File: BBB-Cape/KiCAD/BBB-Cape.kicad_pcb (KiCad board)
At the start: 2 copper layers, 75.3 x 54.6 mm, 60 parts, among them J1 01x06_Stackable Header, J2 RJ45-TRANSFO, P8 02x23_Stackable Header, P9 02x23_Stackable Header, SW1 W5500_RST, SW2 SYS_RST, SW3 Power, U1 WIZnet W5500, Y1 25MHz

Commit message: BBB for review
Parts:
- removed I2C1_0, I2C2_0: Conn_01x02, Pin_Headers:Pin_Header_Straight_1x02_Pitch2.54mm_SMD_Pin1Left
- removed P8, P9: 02x23_Stackable Header, Pin_Headers:Pin_Header_Straight_2x23_Pitch2.54mm
- added C18: 0.1uF, Capacitors_SMD:C_0805, F.Cu at (198.9, 99.6)
- added C19: 0.1uF, Capacitors_SMD:C_0805, F.Cu at (206.5, 99.6)
- added C20: 10nF, Capacitors_SMD:C_0805, F.Cu at (191.5, 102.0)
- added C21: 22nF, Capacitors_SMD:C_0805, F.Cu at (205.9, 105.2)
- added C22: 4.7uF, Capacitors_SMD:C_0805, F.Cu at (201.4, 99.6)
- added C23: 10nF, Capacitors_SMD:C_0805, F.Cu at (204.0, 99.6)
- added C24: 18pF, Capacitors_SMD:C_0805, F.Cu at (214.5, 95.4)
- added C25: 18pF, Capacitors_SMD:C_0805, F.Cu at (214.5, 89.7)
- added C26: 0.1uF, Capacitors_SMD:C_0805, F.Cu at (137.2, 124.7)
- added C27: 0.1uF, Capacitors_SMD:C_0805, F.Cu at (142.2, 124.8)
- added D2: 0.455V 20.0A, Diodes_SMD:D_0805, F.Cu at (207.2, 48.3)
- added I2C2_1: Conn_01x02, Pin_Headers:Pin_Header_Straight_1x02_Pitch2.54mm_SMD_Pin1Left, F.Cu at (97.3, 100.4)
- added I2C2_2: Conn_01x02, Pin_Headers:Pin_Header_Straight_1x02_Pitch2.54mm_SMD_Pin1Left, F.Cu at (97.1, 89.1)
- added J10: Conn_01x02, Connectors_Phoenix:PhoenixContact_MC-G_02x3.50mm_Angled, F.Cu at (203.2, 36.8)
- added J11: RJ45-TRANSFO, Connectors:RJ45_TRANSFO, F.Cu at (200.7, 121.3)
- added J12: DB9_Female, Connectors_DSub:DSUB-9_Female_Horizontal_Pitch2.77x2.84mm_EdgePinOffset14.56mm_Housed_MountingHolesOffset15.98mm, F.Cu at (173.0, 118.0)
- added J3: MOUNTING_HOLE, Mounting_Holes:MountingHole_3.2mm_M3_Pad, F.Cu at (122.1, 42.8)
- added J4: MOUNTING_HOLE, Mounting_Holes:MountingHole_3.2mm_M3_Pad, F.Cu at (170.4, 42.6)
- added J5: MOUNTING_HOLE, Mounting_Holes:MountingHole_3.2mm_M3_Pad, F.Cu at (213.3, 137.2)
- added J6: MOUNTING_HOLE, Mounting_Holes:MountingHole_3.2mm_M3_Pad, F.Cu at (213.4, 28.8)
- added J7: MOUNTING_HOLE, Mounting_Holes:MountingHole_3.2mm_M3_Pad, F.Cu at (77.1, 137.2)
- added J8: MOUNTING_HOLE, Mounting_Holes:MountingHole_3.2mm_M3_Pad, F.Cu at (77.2, 28.8)
- added J9: 01x06_Stackable Header, Pin_Headers:Pin_Header_Straight_1x06_Pitch2.54mm, B.Cu at (165.0, 70.7)
- added L1: 27.0uH, Inductors_SMD:L_Wuerth_HCM-1240, F.Cu at (200.0, 62.0)
- added L2: BLM21PG121SN1D, Inductors_SMD:L_0805_HandSoldering, F.Cu at (192.5, 73.8)
- added P1: 02x23_Stackable Header, Pin_Headers:Pin_Header_Straight_2x23_Pitch2.54mm, B.Cu at (171.7, 47.8)
- added P2: 02x23_Stackable Header, Pin_Headers:Pin_Header_Straight_2x23_Pitch2.54mm, B.Cu at (123.4, 47.8)
- added P3: 02x23_Stackable Header, Pin_Headers:Pin_Header_Straight_2x23_Pitch2.54mm, B.Cu at (112.8, 47.2)
- added P4: 02x23_Stackable Header, Pin_Headers:Pin_Header_Straight_2x23_Pitch2.54mm, B.Cu at (182.1, 48.0)
- added R22: 10k, Resistors_SMD:R_0805, F.Cu at (211.3, 78.9)
- added R23: 10k, Resistors_SMD:R_0805, F.Cu at (210.0, 98.6)
- added R24: 10k, Resistors_SMD:R_0805, F.Cu at (207.8, 83.6)
- added R25: 10M, Resistors_SMD:R_0805, F.Cu at (214.1, 92.5)
- added R26: 20k, Resistors_SMD:R_0805, F.Cu at (140.0, 134.0)
- added R27: 20k, Resistors_SMD:R_0805, F.Cu at (132.4, 124.5)
- added R28: 0, Resistors_SMD:R_0805, F.Cu at (132.4, 127.6)
- added R29: 0, Resistors_SMD:R_0805, F.Cu at (132.4, 132.7)
- added R30: 0, Resistors_SMD:R_0805, F.Cu at (132.4, 135.3)
- added R31: 0, Resistors_SMD:R_0805, F.Cu at (132.4, 130.2)
- added R32: 120, Resistors_SMD:R_0805, F.Cu at (145.4, 127.3)
- added R33: 120, Resistors_SMD:R_0805, F.Cu at (145.4, 131.1)
- added REF**: Paradigm Logo Very Small, Paradigm_Logo_Very_Small, F.Cu at (134.6, 64.5)
- added U2: WIZnet W5500, Housings_QFP:LQFP-48_7x7mm_Pitch0.5mm, F.Cu at (202.0, 91.8)
- added U3: MAX13433EETD, Housings_DFN_QFN:DFN-14-1EP_3x4mm_Pitch0.5mm, F.Cu at (139.5, 129.5)
- C1: value 10uF -> 1.00uF; footprint Capacitors_SMD:CP_Elec_3x5.3 -> Capacitors_SMD:C_0805
- C10: value 6.8nF -> 0.1uF
- C11: value 6.8nF -> 10uF; footprint Capacitors_SMD:C_0805 -> Capacitors_SMD:CP_Elec_3x5.3
- C12, C15: value 10nF -> 0.1uF
- C13: value 22nF -> 0.1uF
- C14: value 4.7uF -> 0.1uF
- C16, C17: value 18pF -> 6.8nF
- C3: value 10uF -> 270pF; footprint Capacitors_SMD:CP_Elec_3x5.3 -> Capacitors_SMD:C_0805
- C4: value 0.1uF -> 1.80nF
- C5: value 0.1uF -> 22nF
- C6: value 0.1uF -> 8.2nF
- C7, C8: value 0.1uF -> 47uF
- C9: value 0.1uF -> 10uF; footprint Capacitors_SMD:C_0805 -> Capacitors_SMD:CP_Elec_3x5.3
- J1: value 01x06_Stackable Header -> MOUNTING_HOLE; footprint Pin_Headers:Pin_Header_Straight_1x06_Pitch2.54mm -> Mounting_Holes:MountingHole_3.2mm_M3_Pad
- J2: value RJ45-TRANSFO -> MOUNTING_HOLE; footprint Connectors:RJ45_TRANSFO -> Mounting_Holes:MountingHole_3.2mm_M3_Pad
- R1: value 49.9 -> 330
- R10, R11: value 10k -> 82
- R12: value 10k -> 10
- R13: value 10k -> 12.4k
- R2: value 49.9 -> 16.2k
- R20: value 10M -> 10k
- R21: value 330 -> 10k
- R3: value 10 -> 22.1k
- R4: value 330 -> 3.09k
- R5: value 330 -> 1.02k
- R6: value 82 -> 49.9
- R7: value 82 -> 330
- R8: value 12.4k -> 330
- R9: value 10k -> 49.9
- U1: value WIZnet W5500 -> LM25576MH; footprint Housings_QFP:LQFP-48_7x7mm_Pitch0.5mm -> Housings_SSOP:HTSSOP-20-1EP_4.4x6.5mm_Pitch0.65mm_ThermalPad; moved to F.Cu
- moved SW2 119.0 mm to (188.0, 33.9), turned to 90 degrees
- moved SW1 118.1 mm to (212.2, 82.9), turned to 90 degrees
- moved SW3 112.7 mm to (182.9, 33.9), turned to 90 degrees
- moved D1 109.2 mm to (180.8, 39.8)
- moved R21 102.8 mm to (205.2, 79.8), turned to 270 degrees
- moved U1 88.9 mm to (200.6, 46.3)
- moved UART5 84.7 mm to (86.7, 129.8)
- moved PWR1 69.2 mm to (80.6, 51.4), turned to 180 degrees
- moved SPI1_1 62.6 mm to (80.8, 96.8)
- moved C2 61.0 mm to (192.0, 40.0), turned to 180 degrees
- moved R1 60.8 mm to (184.9, 39.9), turned to 90 degrees
- moved C4 60.2 mm to (189.6, 45.7)
- moved UART3 60.0 mm to (99.6, 130.3)
- moved UART4 58.9 mm to (97.6, 114.0), turned to 0 degrees
- moved C1 57.5 mm to (192.0, 43.2), turned to 180 degrees
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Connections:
- C1 pad 1: 3V3D -> Net-(C1-Pad1)
- C1 pad 2: Net-(C1-Pad2) -> DGND
- C10 pad 1: Net-(C10-Pad1) -> VDD_3V3
- C10 pad 2: RX+ -> DGND
- C11 pad 1: Net-(C11-Pad1) -> 3V3D
- C11 pad 2: RX- -> Net-(C11-Pad2)
- C12 pad 1: Net-(C12-Pad1) -> VDD_3V3
- C13 pad 1: Net-(C13-Pad1) -> 3V3D
- C13 pad 2: DGND -> Net-(C11-Pad2)
- C14 pad 1: Net-(C14-Pad1) -> VDD_3V3
- C15 pad 1: Net-(C15-Pad1) -> VDD_3V3
- C16 pad 2: DGND -> RX+
- C17 pad 2: DGND -> RX-
- C2 pad 1: 3V3D -> Net-(C2-Pad1)
- C2 pad 2: Net-(C1-Pad2) -> DGND
- C3 pad 1: VDD_3V3 -> Net-(C3-Pad1)
- C4 pad 1: VDD_3V3 -> Net-(C4-Pad1)
- C4 pad 2: DGND -> Net-(C4-Pad2)
- C5 pad 1: VDD_3V3 -> Net-(C5-Pad1)
- C5 pad 2: DGND -> Net-(C5-Pad2)
- C6 pad 1: VDD_3V3 -> Net-(C6-Pad1)
- C7 pad 1: VDD_3V3 -> VDD_5V
- C7 pad 2: DGND -> Net-(C7-Pad2)
- C8 pad 1: VDD_3V3 -> Net-(C7-Pad2)
- J2 pad 1: TX+ -> DGND
- R1 pad 1: VDD_3V3 -> Net-(D1-Pad1)
- R1 pad 2: TX+ -> DGND
- R10 pad 1: VDD_3V3 -> RX-
- R10 pad 2: Net-(R10-Pad2) -> Net-(C20-Pad1)
- R11 pad 1: VDD_3V3 -> RX+
- R11 pad 2: Net-(R11-Pad2) -> Net-(C20-Pad1)
- R12 pad 2: Net-(R12-Pad2) -> Net-(C21-Pad1)
- R13 pad 1: DGND -> Net-(R13-Pad1)
- R13 pad 2: Net-(R13-Pad2) -> DGND
- R14 pad 1: DGND -> VDD_3V3
- R15 pad 1: DGND -> VDD_3V3
- R16 pad 1: DGND -> VDD_3V3
- R18 pad 1: VDD_3V3 -> DGND
- R18 pad 2: W5500_RST -> Net-(R18-Pad2)
- R19 pad 1: 3V3D -> DGND
- R19 pad 2: W5500_INT -> Net-(R19-Pad2)
- R2 pad 1: VDD_3V3 -> DGND
- R2 pad 2: TX- -> Net-(R2-Pad2)
- R20 pad 1: Net-(C16-Pad1) -> DGND
- R20 pad 2: Net-(C17-Pad1) -> Net-(R20-Pad2)
- R21 pad 1: Net-(D1-Pad1) -> DGND
- R21 pad 2: DGND -> Net-(R21-Pad2)
- R3 pad 1: VDD_3V3 -> Net-(R3-Pad1)
- R3 pad 2: Net-(C13-Pad1) -> Net-(C4-Pad2)
- R4 pad 1: ACT_LED -> Net-(C4-Pad1)
- R4 pad 2: Net-(J2-PadGK) -> VDD_5V
- R5 pad 1: LINK_LED -> DGND
- R5 pad 2: Net-(J2-PadYK) -> Net-(C4-Pad1)
- R6 pad 1: RX- -> VDD_3V3
- R6 pad 2: Net-(C12-Pad1) -> TX+
- R7 pad 1: RX+ -> ACT_LED
- R7 pad 2: Net-(C12-Pad1) -> Net-(J11-PadGK)
- R8 pad 1: Net-(R8-Pad1) -> LINK_LED
- R8 pad 2: DGND -> Net-(J11-PadYK)
- R9 pad 1: DGND -> VDD_3V3
- R9 pad 2: Net-(R9-Pad2) -> TX-
- U1 pad 1: TX- -> Net-(C2-Pad1)
- U1 pad 10: Net-(R8-Pad1) -> DGND
- U1 pad 11: VDD_3V3 -> Net-(C6-Pad1)
- U1 pad 12: Net-(U1-Pad12) -> VDD_5V
- U1 pad 13: Net-(U1-Pad13) -> DGND
- U1 pad 15: VDD_3V3 -> Net-(D2-Pad2)
- U1 pad 16: DGND -> Net-(D2-Pad2)
- U1 pad 17: VDD_3V3 -> Net-(C5-Pad1)
- U1 pad 18: Net-(U1-Pad18) -> Net-(C5-Pad1)
- U1 pad 19: DGND -> Net-(C5-Pad1)
- U1 pad 2: TX+ -> Net-(U1-Pad2)
- U1 pad 20: Net-(C14-Pad1) -> Net-(C5-Pad2)
- U1 pad 21: VDD_3V3 -> (no net)
- U1 pad 3: DGND -> Net-(C1-Pad1)
- U1 pad 4: VDD_3V3 -> Net-(C1-Pad1)
- U1 pad 5: RX- -> Net-(U1-Pad5)
- U1 pad 6: RX+ -> Net-(R3-Pad1)
- U1 pad 7: Net-(U1-Pad7) -> Net-(C4-Pad1)
- U1 pad 8: VDD_3V3 -> Net-(R2-Pad2)
- U1 pad 9: DGND -> Net-(C3-Pad1)
- Y1 pad 1: Net-(C16-Pad1) -> Net-(C24-Pad1)
- Y1 pad 2: Net-(C17-Pad1) -> Net-(C25-Pad1)
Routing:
- net VDD_3V3: track 0.00 -> 342.2 mm, vias 0 -> 13
- net VDD_5V: track 0.00 -> 324.9 mm, vias 0 -> 8
- net DGND: track 0.00 -> 222.5 mm, vias 0 -> 25
- net I2C1_SCL/SPI0_CS0: track 0.00 -> 219.1 mm, vias 0 -> 3
- net EHRPWM1B: track 0.00 -> 178.7 mm, vias 0 -> 4
- net GPIO_115: track 0.00 -> 177.0 mm, vias 0 -> 4
- net EHRPWM1A: track 0.00 -> 172.7 mm, vias 0 -> 4
- net GPIO_117: track 0.00 -> 169.6 mm, vias 0 -> 4
- net GPIO49: track 0.00 -> 160.9 mm, vias 0 -> 4
- net SPI1_CS0: track 0.00 -> 157.9 mm, vias 0 -> 10
- net SPI1_SCLK: track 0.00 -> 157.7 mm, vias 0 -> 9
- net SPI1_D0: track 0.00 -> 155.9 mm, vias 0 -> 8
- net SPI1_DI: track 0.00 -> 154.6 mm, vias 0 -> 11
- net I2C2_SDA/SPIO_SCLK/UART2_RXD: track 0.00 -> 149.9 mm, vias 0 -> 10
- net I2C2_SCL/SPI0_DO/UART2_TXD: track 0.00 -> 138.1 mm, vias 0 -> 10
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- added copper zone on B.Cu, net DGND
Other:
- board size 75.3 x 54.6 mm -> 147.3 x 119.4 mm
- net class Default: clearance 0.254 -> 0.2; trace_width 0.254 -> 0.4064
- net class Signal added: clearance 0.1, trace_width 0.2, via_dia 0.6858, via_drill 0.3302
- net class VCC added: clearance 0.254, trace_width 0.508, via_dia 0.6858, via_drill 0.3302
- rule trace_clearance: 0.254 -> 0.2
- board text added: "Paradigm Hyperloop BBB Socket V1"

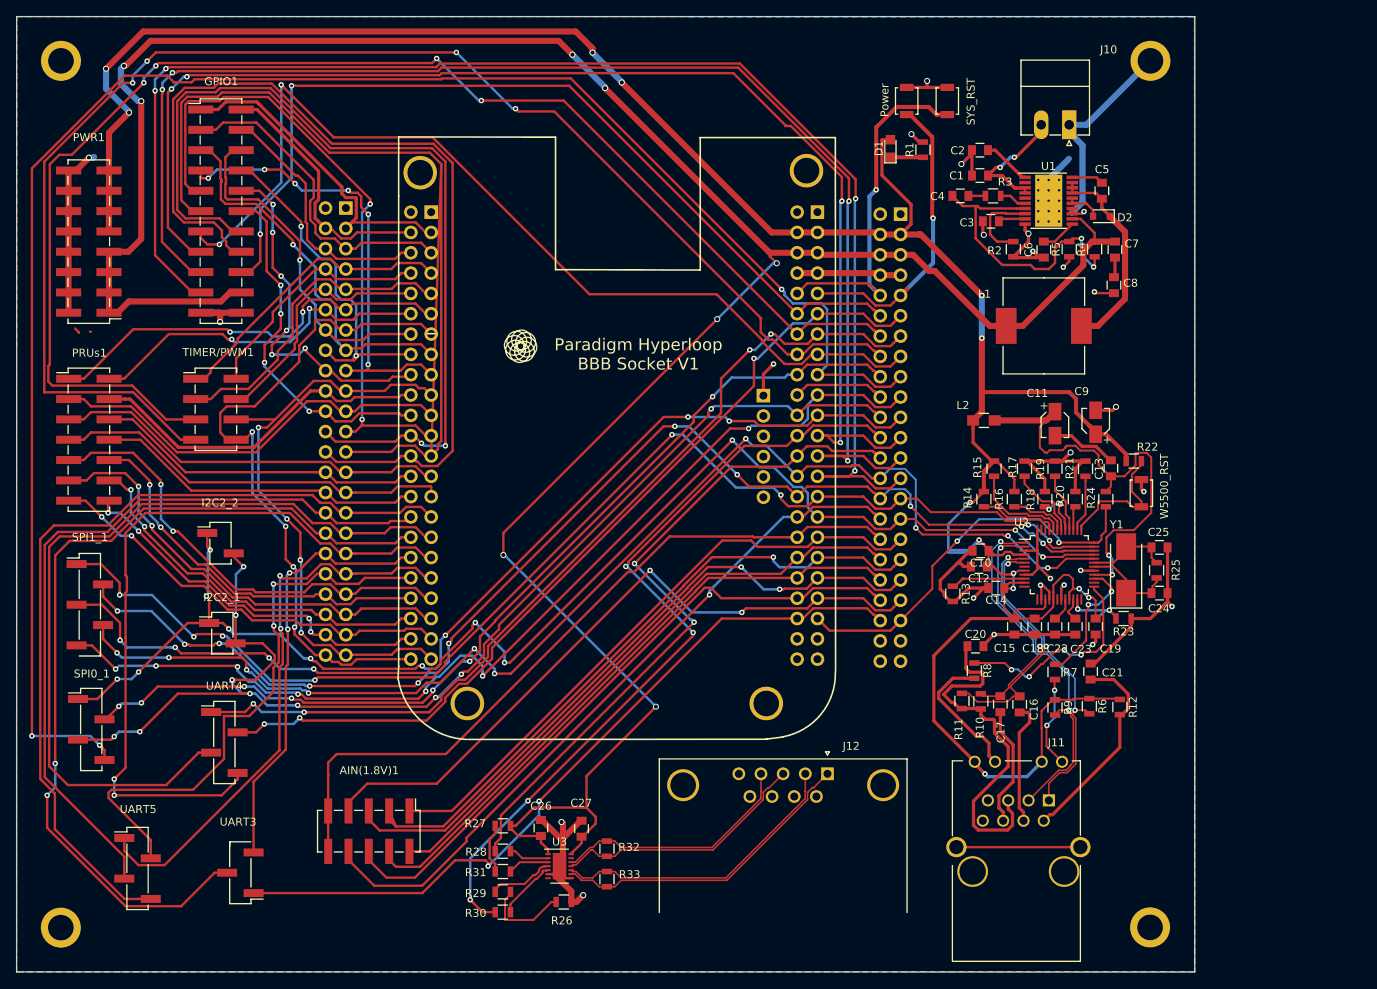
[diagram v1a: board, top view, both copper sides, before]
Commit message: Cape Routing Fixes
General cleanup and optimization.
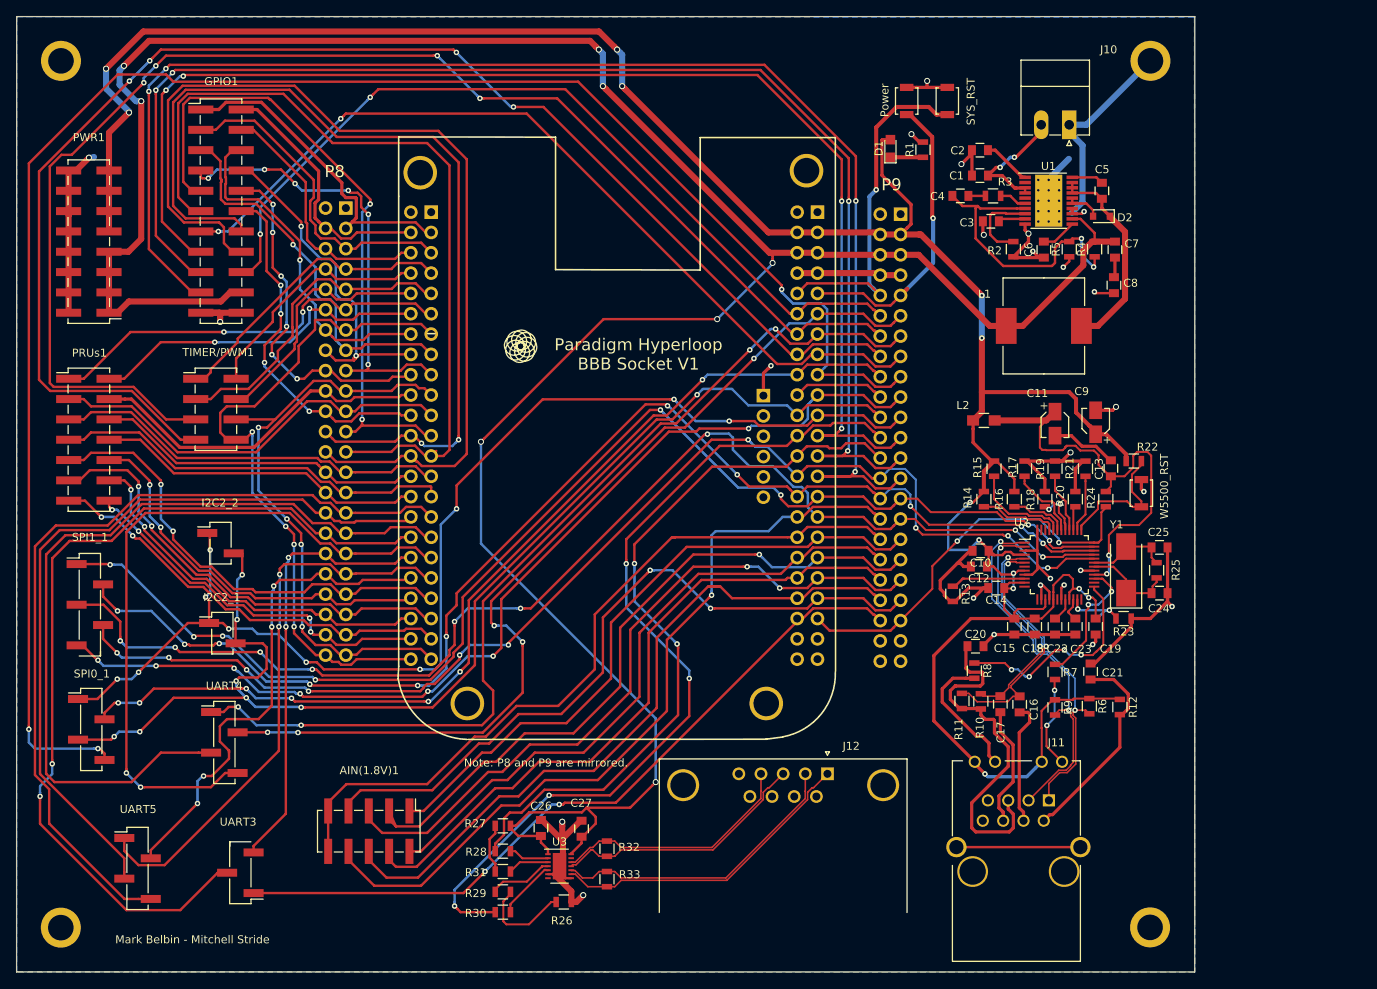
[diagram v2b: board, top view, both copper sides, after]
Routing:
- net GPIO_32: track 137.0 -> 104.0 mm
- net VDD_5V: track 324.9 -> 340.5 mm
- net GPIO_48: track 120.3 -> 108.2 mm
- net I2C2_SCL/SPI0_DO/UART2_TXD: track 138.1 -> 149.9 mm
- net UART4_RXD: track 109.1 -> 118.9 mm, vias 3 -> 5
- net VDD_ADC: track 89.7 -> 99.2 mm
- net I2C1_SCL/UART1_TXD: track 100.4 -> 109.7 mm
- net UART5_RXD+: track 71.9 -> 63.2 mm, vias 2 -> 4
- net UART4_TXD: track 112.4 -> 120.4 mm
- net GPIO_60: track 113.1 -> 106.1 mm
- net AIN1: track 82.6 -> 89.1 mm
- net SPI1_DI: track 154.6 -> 160.0 mm
- net I2C1_SDA/UART1_RXD: track 86.8 -> 92.2 mm
- net UART4_CTSn: track 92.8 -> 87.5 mm
- net AIN3: track 79.0 -> 84.1 mm
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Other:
- board text added: "Mark Belbin - Mitchell Stride"
- board text added: "Note: P8 and P9 are mirrored."
- board text added: "P8"
- board text added: "P9"
